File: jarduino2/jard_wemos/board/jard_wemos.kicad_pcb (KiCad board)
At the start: 2 copper layers, 57 x 42 mm, 32 parts, among them J1 Conn_01x05, J2 LEDs, Q1 BPC_IPP034N03L, U1 BPC_Alim5V, U2 WeMos_D1_mini, U3 24LC01

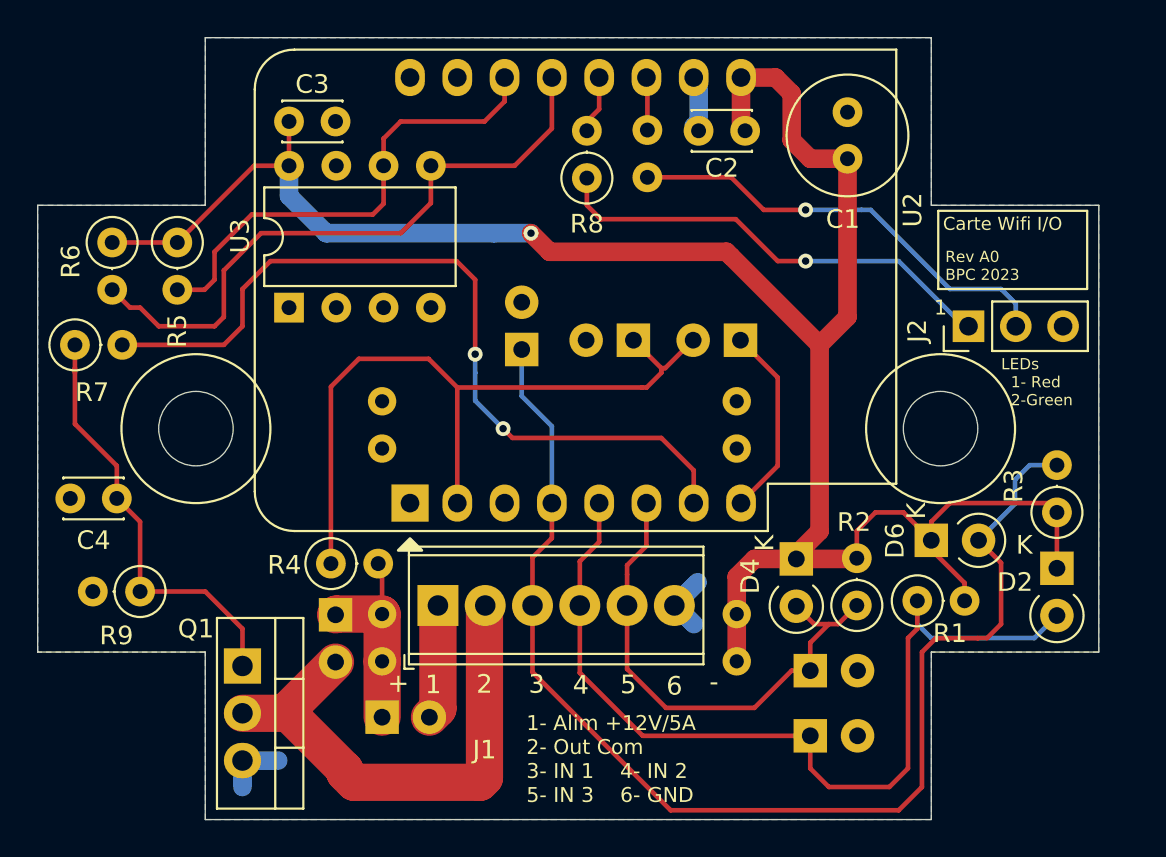
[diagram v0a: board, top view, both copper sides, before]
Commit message: Agrandissement des trous du module alim Changement de face de R8
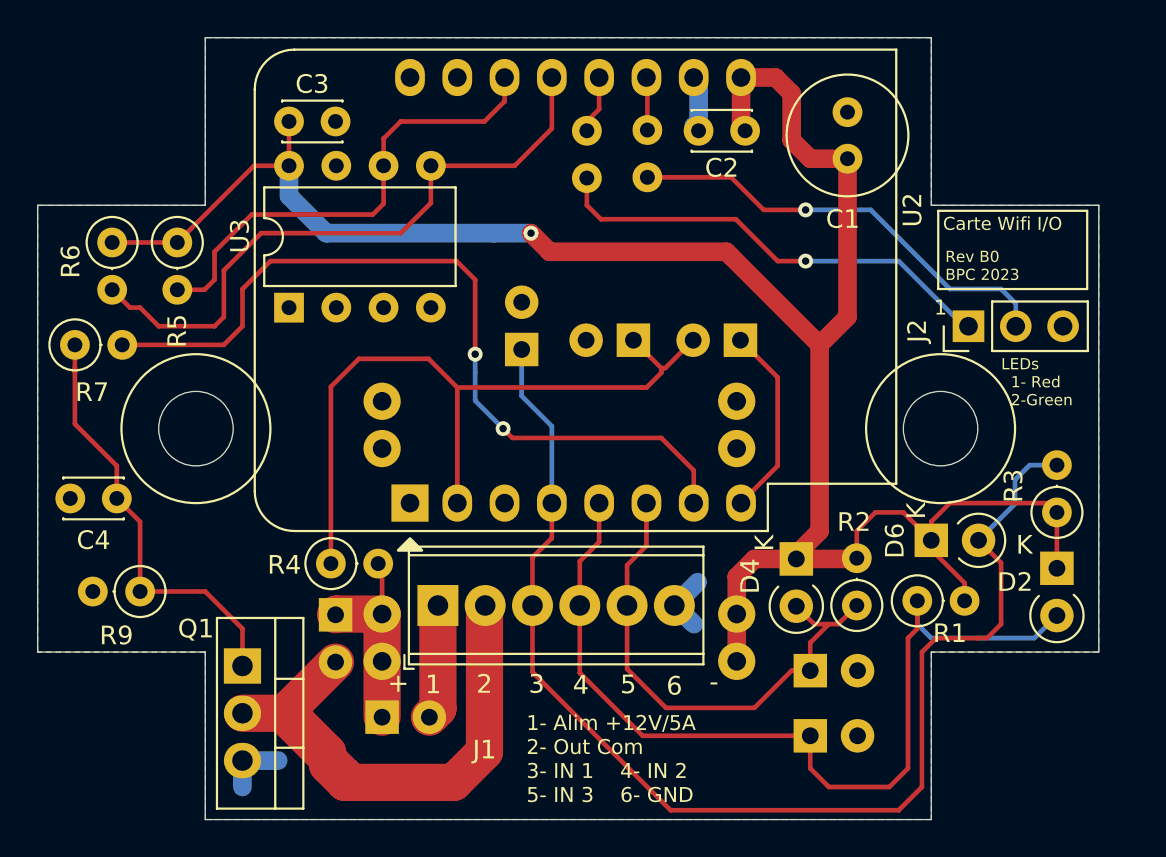
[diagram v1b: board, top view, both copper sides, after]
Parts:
- R8: moved to B.Cu
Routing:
- net OUT_12V_COM: track 27.8 -> 32.4 mm
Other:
- board text added: "Rev B0 BPC 2023"
- board text removed: "Rev A0 BPC 2023"

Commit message: Changement alim 5V -> 3.3V
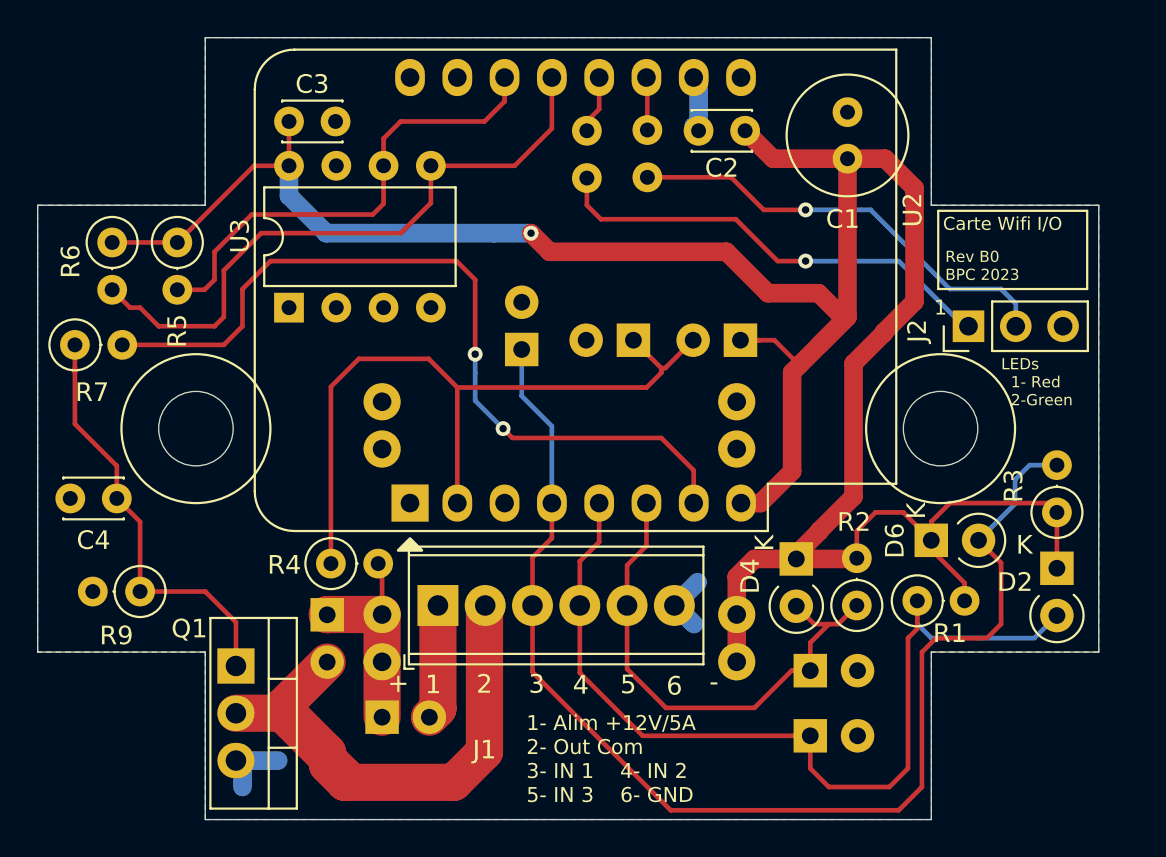
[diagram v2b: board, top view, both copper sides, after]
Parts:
- U1: value BPC_Alim5V -> BPC_Alim3_3V; footprint bpc:BPC_Alim5V -> bpc:BPC_Alim3_3V
- moved D10 0.45 mm to (137.6, 119.5)
- moved Q1 0.35 mm to (132.7, 122.2)
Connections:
- C1 pad 1: +5V -> +3V3
- C2 pad 1: +5V -> +3V3
- C3 pad 2: +5V -> +3V3
- D2 pad 1: +5V -> +3V3
- D4 pad 1: +5V -> +3V3
- D6 pad 1: +5V -> +3V3
- D8 pad 1: Net-(D8-Pad1) -> +3V3
- R1 pad 2: +5V -> +3V3
- R2 pad 2: +5V -> +3V3
- R3 pad 1: +5V -> +3V3
- R5 pad 1: +5V -> +3V3
- R6 pad 1: +5V -> +3V3
- U1 pad 7: +5V -> +3V3
- U1 pad 8: +5V -> +3V3
- U2 pad 8: Net-(D8-Pad1) -> +3V3
- U2 pad 9: +5V -> Net-(U2-Pad9)
- U3 pad 8: +5V -> +3V3
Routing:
- net +3V3: track 0.00 -> 144.9 mm, vias 0 -> 1
- net +5V: track 116.9 -> 0.00 mm, vias 1 -> 0
- net Net-(D8-Pad1): track 10.4 -> 0.00 mm
- net OUT_12V_COM: track 32.4 -> 32.9 mm

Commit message: Relier RST et D0 pour la sortie de veille (strap sur A0 et B0)
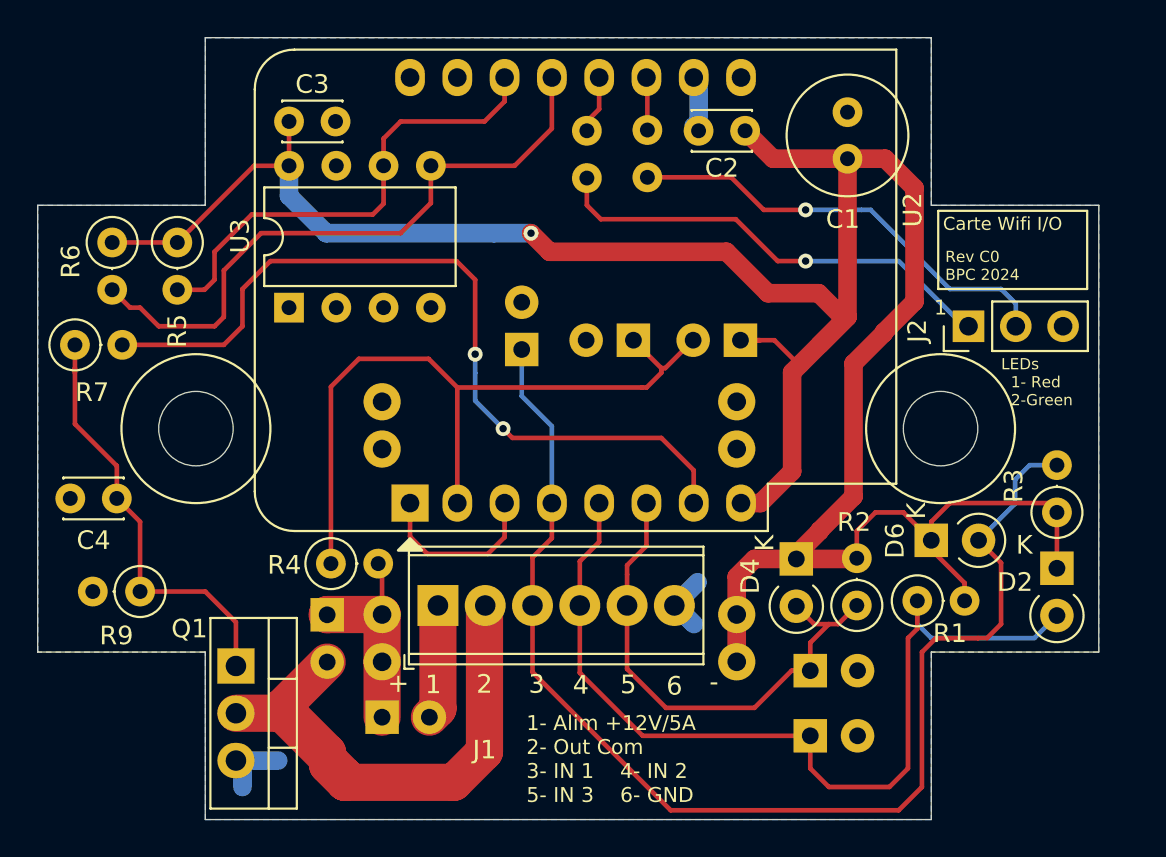
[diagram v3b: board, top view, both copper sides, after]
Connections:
- U2 pad 1: Net-(U2-Pad1) -> RST_D0
- U2 pad 15: Net-(U2-Pad15) -> unconnected-(U2-RX-Pad15)
- U2 pad 16: Net-(U2-Pad16) -> unconnected-(U2-TX-Pad16)
- U2 pad 3: Net-(U2-Pad3) -> RST_D0
- U2 pad 9: Net-(U2-Pad9) -> unconnected-(U2-5V-Pad9)
- U3 pad 1: Net-(U3-Pad1) -> unconnected-(U3-A0-Pad1)
- U3 pad 2: Net-(U3-Pad2) -> unconnected-(U3-A1-Pad2)
- U3 pad 3: Net-(U3-Pad3) -> unconnected-(U3-A2-Pad3)
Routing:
- net RST_D0: track 0.00 -> 9.47 mm
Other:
- net class Default removed
- board text added: "Rev C0 BPC 2024"
- board text removed: "Rev B0 BPC 2023"
